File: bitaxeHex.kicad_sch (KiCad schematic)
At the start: 20 parts, among them J1 Screw Terminal, J2 Conn_01x01

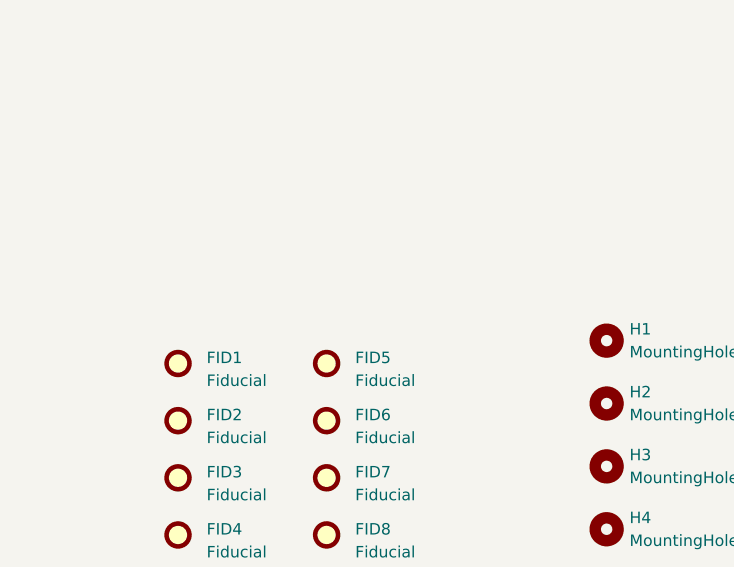
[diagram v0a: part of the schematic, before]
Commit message: link heatsink to schematic and re-link heatsink mounting holes :P
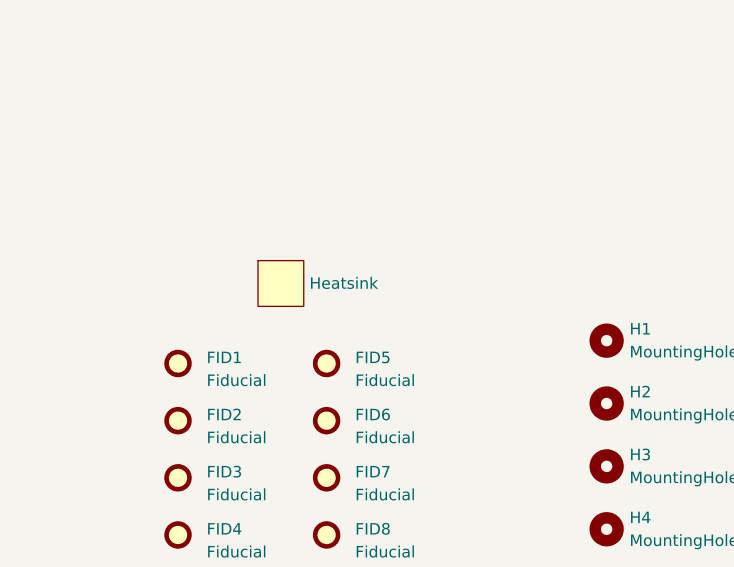
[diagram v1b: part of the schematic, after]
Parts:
- added HS1: Heatsink, bitaxe:hex-heatsink, symbol bitaxe:heatsink
- H10, H5, H6, H7, H8, H9: footprint bitaxe:2.5mm_mounting -> bitaxe:2.2mm_mounting
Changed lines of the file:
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@@
     (pin "1")
     (instances
-      (project "bitaxeUltraHex"
+      (project "bitaxeHex"
         (path "/e63e39d7-6ac0-4ffd-8aa3-1841a4541b55"
           (reference "J1") (unit 1)
@@
     )
     (instances
-      (project "bitaxeUltraHex"
+      (project "bitaxeHex"
         (path "/e63e39d7-6ac0-4ffd-8aa3-1841a4541b55"
           (reference "FID5") (unit 1)
@@
     )
     (instances
-      (project "bitaxeUltraHex"
+      (project "bitaxeHex"
         (path "/e63e39d7-6ac0-4ffd-8aa3-1841a4541b55"
           (reference "H4") (unit 1)
@@
     )
     (instances
-      (project "bitaxeUltraHex"
+      (project "bitaxeHex"
         (path "/e63e39d7-6ac0-4ffd-8aa3-1841a4541b55"
           (reference "H1") (unit 1)
@@
     )
     (instances
-      (project "bitaxeUltraHex"
+      (project "bitaxeHex"
         (path "/e63e39d7-6ac0-4ffd-8aa3-1841a4541b55"
           (reference "H2") (unit 1)
@@
     )
     (instances
-      (project "bitaxeUltraHex"
+      (project "bitaxeHex"
         (path "/e63e39d7-6ac0-4ffd-8aa3-1841a4541b55"
           (reference "#G1") (unit 1)
@@
     )
     (instances
-      (project "bitaxeUltraHex"
+      (project "bitaxeHex"
         (path "/e63e39d7-6ac0-4ffd-8aa3-1841a4541b55"
           (reference "H3") (unit 1)
@@
     )
     (instances
-      (project "bitaxeUltraHex"
+      (project "bitaxeHex"
         (path "/e63e39d7-6ac0-4ffd-8aa3-1841a4541b55"
           (reference "FID6") (unit 1)
@@
       (effects (font (size 1.27 1.27)) (justify left))
     )
-    (property "Footprint" "bitaxe:2.5mm_mounting" (at 118.745 164.465 0)
+    (property "Footprint" "bitaxe:2.2mm_mounting" (at 118.745 164.465 0)
       (effects (font (size 1.27 1.27)) hide)
     )
@@
     )
     (instances
-      (project "bitaxeUltraHex"
+      (project "bitaxeHex"
         (path "/e63e39d7-6ac0-4ffd-8aa3-1841a4541b55"
           (reference "H6") (unit 1)
@@
     )
   )
+  (symbol (lib_id "bitaxe:heatsink") (at 48.895 163.195 0) (unit 1)
+    (in_bom no) (on_board yes) (dnp no) (fields_autoplaced)
+    (property "Reference" "HS1" (at 48.895 163.195 0)
+      (effects (font (size 1.27 1.27)) hide)
+    )
+    (property "Value" "Heatsink" (at 52.07 163.195 0)
+      (effects (font (size 1.27 1.27)) (justify left))
+    )
+    (property "Footprint" "bitaxe:hex-heatsink" (at 50.165 169.545 0)
+      (effects (font (size 1.27 1.27)) hide)
+    )
+    (property "Datasheet" "" (at 48.895 163.195 0)
+      (effects (font (size 1.27 1.27)) hide)
+    )
+    (instances
+      (project "bitaxeHex"
+        (path "/e63e39d7-6ac0-4ffd-8aa3-1841a4541b55"
+          (reference "HS1") (unit 1)
+        )
+      )
+    )
+  )
   (symbol (lib_id "Mechanical:Fiducial") (at 53.975 184.785 0) (unit 1)
     (in_bom no) (on_board yes) (dnp no) (fields_autoplaced)
@@
     )
     (instances
-      (project "bitaxeUltraHex"
+      (project "bitaxeHex"
         (path "/e63e39d7-6ac0-4ffd-8aa3-1841a4541b55"
           (reference "FID7") (unit 1)
@@
     (pin "1")
     (instances
-      (project "bitaxeUltraHex"
+      (project "bitaxeHex"
         (path "/e63e39d7-6ac0-4ffd-8aa3-1841a4541b55"
           (reference "J2") (unit 1)
@@
       (effects (font (size 1.27 1.27)) (justify left))
     )
-    (property "Footprint" "bitaxe:2.5mm_mounting" (at 118.745 170.815 0)
+    (property "Footprint" "bitaxe:2.2mm_mounting" (at 118.745 170.815 0)
       (effects (font (size 1.27 1.27)) hide)
     )
@@
     )
     (instances
-      (project "bitaxeUltraHex"
+      (project "bitaxeHex"
         (path "/e63e39d7-6ac0-4ffd-8aa3-1841a4541b55"
           (reference "H7") (unit 1)
@@
     )
     (instances
-      (project "bitaxeUltraHex"
+      (project "bitaxeHex"
         (path "/e63e39d7-6ac0-4ffd-8aa3-1841a4541b55"
           (reference "FID3") (unit 1)
@@
       (effects (font (size 1.27 1.27)) (justify left))
     )
-    (property "Footprint" "bitaxe:2.5mm_mounting" (at 118.745 158.115 0)
+    (property "Footprint" "bitaxe:2.2mm_mounting" (at 118.745 158.115 0)
       (effects (font (size 1.27 1.27)) hide)
     )
@@
     )
     (instances
-      (project "bitaxeUltraHex"
+      (project "bitaxeHex"
         (path "/e63e39d7-6ac0-4ffd-8aa3-1841a4541b55"
           (reference "H5") (unit 1)
@@
     )
     (instances
-      (project "bitaxeUltraHex"
+      (project "bitaxeHex"
         (path "/e63e39d7-6ac0-4ffd-8aa3-1841a4541b55"
           (reference "FID8") (unit 1)
@@
       (effects (font (size 1.27 1.27)) (justify left))
     )
-    (property "Footprint" "bitaxe:2.5mm_mounting" (at 118.745 177.165 0)
+    (property "Footprint" "bitaxe:2.2mm_mounting" (at 118.745 177.165 0)
       (effects (font (size 1.27 1.27)) hide)
     )
@@
     )
     (instances
-      (project "bitaxeUltraHex"
+      (project "bitaxeHex"
         (path "/e63e39d7-6ac0-4ffd-8aa3-1841a4541b55"
           (reference "H8") (unit 1)
@@
     )
     (instances
-      (project "bitaxeUltraHex"
+      (project "bitaxeHex"
         (path "/e63e39d7-6ac0-4ffd-8aa3-1841a4541b55"
           (reference "FID2") (unit 1)
@@
     )
     (instances
-      (project "bitaxeUltraHex"
+      (project "bitaxeHex"
         (path "/e63e39d7-6ac0-4ffd-8aa3-1841a4541b55"
           (reference "FID4") (unit 1)
@@
     )
     (instances
-      (project "bitaxeUltraHex"
+      (project "bitaxeHex"
         (path "/e63e39d7-6ac0-4ffd-8aa3-1841a4541b55"
           (reference "FID1") (unit 1)
@@
       (effects (font (size 1.27 1.27)) (justify left))
     )
-    (property "Footprint" "bitaxe:2.5mm_mounting" (at 118.745 190.5 0)
+    (property "Footprint" "bitaxe:2.2mm_mounting" (at 118.745 190.5 0)
       (effects (font (size 1.27 1.27)) hide)
     )
@@
     )
     (instances
-      (project "bitaxeUltraHex"
+      (project "bitaxeHex"
         (path "/e63e39d7-6ac0-4ffd-8aa3-1841a4541b55"
           (reference "H10") (unit 1)
@@
       (effects (font (size 1.27 1.27)) (justify left))
     )
-    (property "Footprint" "bitaxe:2.5mm_mounting" (at 118.745 184.15 0)
+    (property "Footprint" "bitaxe:2.2mm_mounting" (at 118.745 184.15 0)
       (effects (font (size 1.27 1.27)) hide)
     )
@@
     )
     (instances
-      (project "bitaxeUltraHex"
+      (project "bitaxeHex"
         (path "/e63e39d7-6ac0-4ffd-8aa3-1841a4541b55"
           (reference "H9") (unit 1)
@@
     )
     (instances
-      (project "bitaxeUltraHex"
+      (project "bitaxeHex"
         (path "/e63e39d7-6ac0-4ffd-8aa3-1841a4541b55" (page "5"))
       )
@@
     )
     (instances
-      (project "bitaxeUltraHex"
+      (project "bitaxeHex"
         (path "/e63e39d7-6ac0-4ffd-8aa3-1841a4541b55" (page "6"))
       )
@@
     )
     (instances
-      (project "bitaxeUltraHex"
+      (project "bitaxeHex"
         (path "/e63e39d7-6ac0-4ffd-8aa3-1841a4541b55" (page "4"))
       )
@@
     )
     (instances
-      (project "bitaxeUltraHex"
+      (project "bitaxeHex"
         (path "/e63e39d7-6ac0-4ffd-8aa3-1841a4541b55" (page "2"))
       )
@@
     )
     (instances
-      (project "bitaxeUltraHex"
+      (project "bitaxeHex"
         (path "/e63e39d7-6ac0-4ffd-8aa3-1841a4541b55" (page "3"))
       )
@@
     )
     (instances
-      (project "bitaxeUltraHex"
+      (project "bitaxeHex"
         (path "/e63e39d7-6ac0-4ffd-8aa3-1841a4541b55" (page "7"))
       )

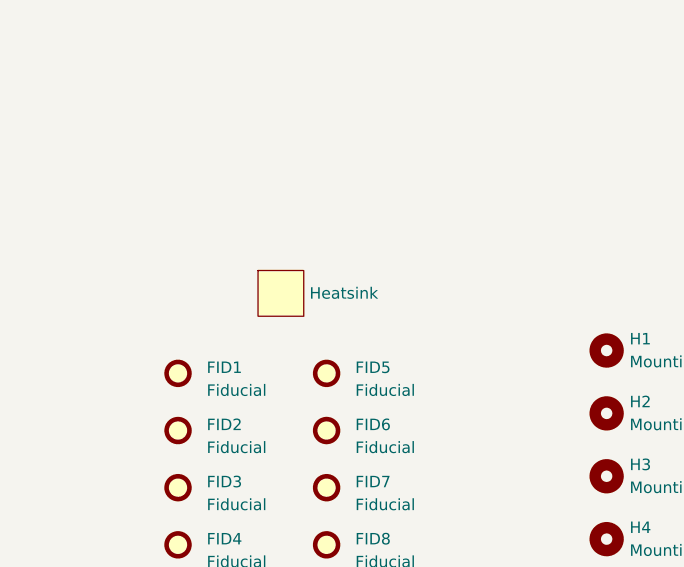
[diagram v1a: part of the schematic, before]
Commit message: silkscreen cleanup
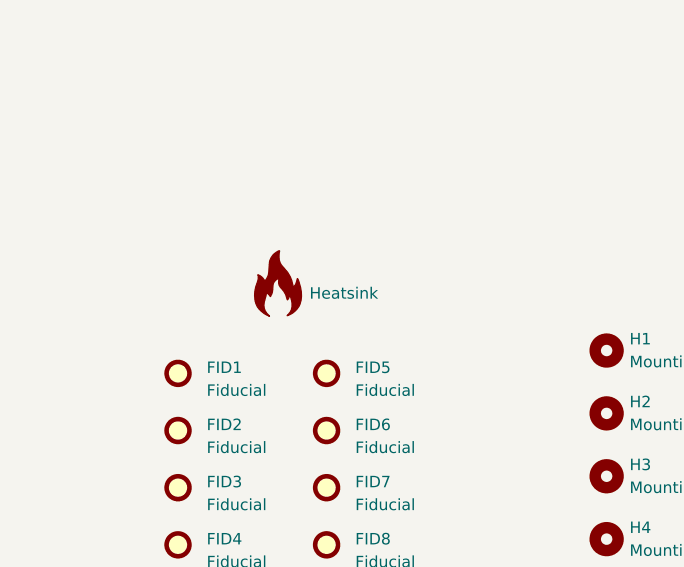
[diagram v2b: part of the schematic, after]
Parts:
- HS1: symbol bitaxe:heatsink -> bitaxe:hex_heatsink
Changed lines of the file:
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@@
     )
   )
-  (symbol (lib_id "bitaxe:heatsink") (at 48.895 163.195 0) (unit 1)
+  (symbol (lib_id "bitaxe:hex_heatsink") (at 48.895 163.195 0) (unit 1)
     (in_bom no) (on_board yes) (dnp no) (fields_autoplaced)
     (property "Reference" "HS1" (at 48.895 163.195 0)

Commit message: mounting holes and fiducials
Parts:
- H1, H2, H3, H4: footprint bitaxe:4mm_mounting -> MountingHole:MountingHole_3mm_Pad_Via
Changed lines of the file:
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@@
       (effects (font (size 1.27 1.27)) (justify left))
     )
-    (property "Footprint" "bitaxe:4mm_mounting" (at 85.09 190.5 0)
+    (property "Footprint" "MountingHole:MountingHole_3mm_Pad_Via" (at 85.09 190.5 0)
       (effects (font (size 1.27 1.27)) hide)
     )
@@
       (effects (font (size 1.27 1.27)) (justify left))
     )
-    (property "Footprint" "bitaxe:4mm_mounting" (at 85.09 169.545 0)
+    (property "Footprint" "MountingHole:MountingHole_3mm_Pad_Via" (at 85.09 169.545 0)
       (effects (font (size 1.27 1.27)) hide)
     )
@@
       (effects (font (size 1.27 1.27)) (justify left))
     )
-    (property "Footprint" "bitaxe:4mm_mounting" (at 85.09 176.53 0)
+    (property "Footprint" "MountingHole:MountingHole_3mm_Pad_Via" (at 85.09 176.53 0)
       (effects (font (size 1.27 1.27)) hide)
     )
@@
       (effects (font (size 1.27 1.27)) (justify left))
     )
-    (property "Footprint" "bitaxe:4mm_mounting" (at 85.09 183.515 0)
+    (property "Footprint" "MountingHole:MountingHole_3mm_Pad_Via" (at 85.09 183.515 0)
       (effects (font (size 1.27 1.27)) hide)
     )
